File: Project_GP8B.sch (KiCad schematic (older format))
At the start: 15 parts, among them U1 74AHC05, U2 74AHC05, U3 74AHC1G04, U4 74AHC1G04, U5 74AHC05

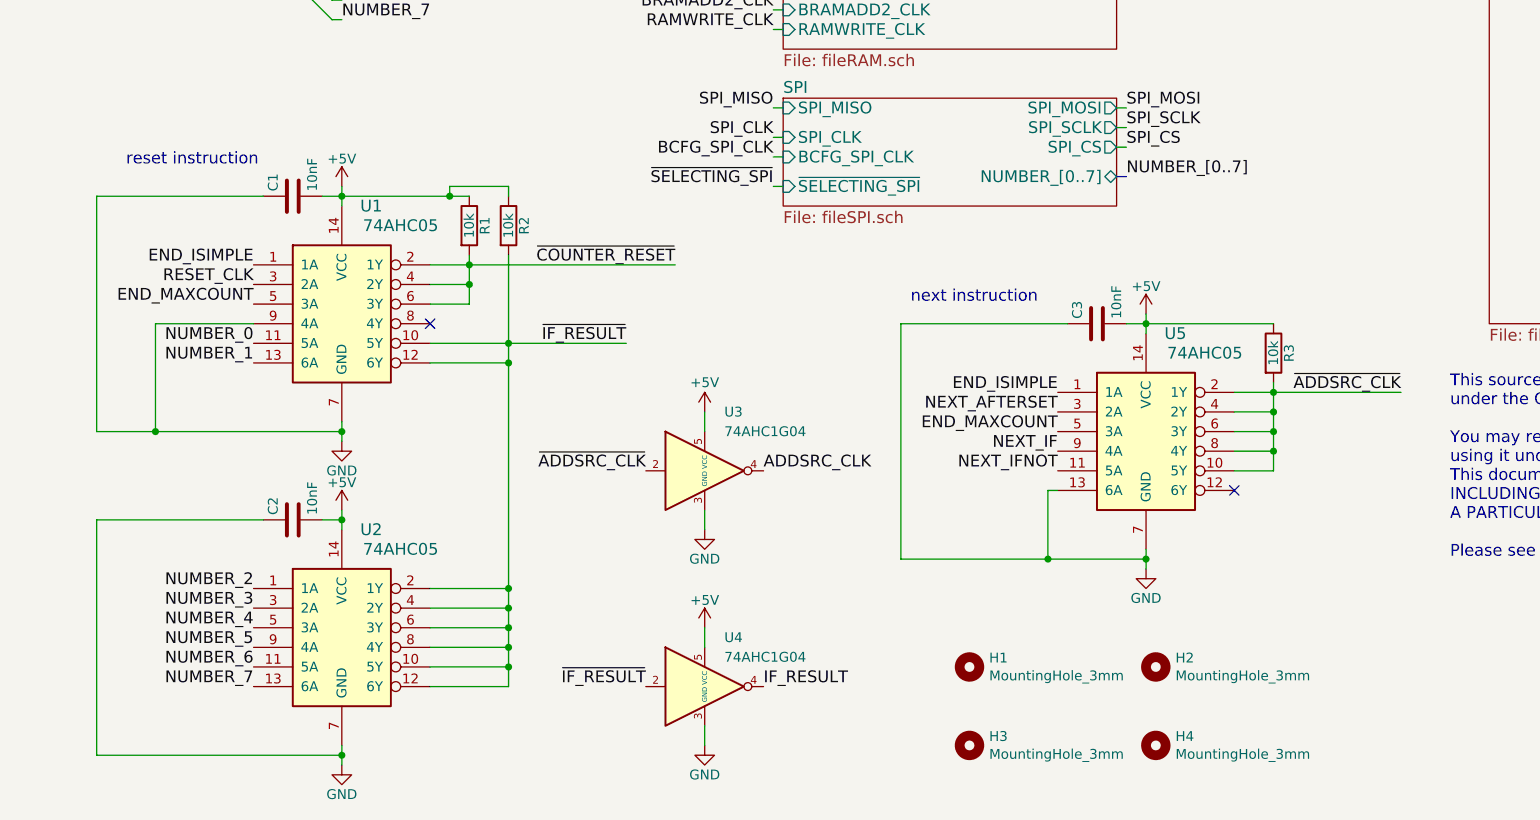
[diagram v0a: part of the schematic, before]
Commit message: Replace some gates with a 74AHC1G02 to fix the pulse problem #3
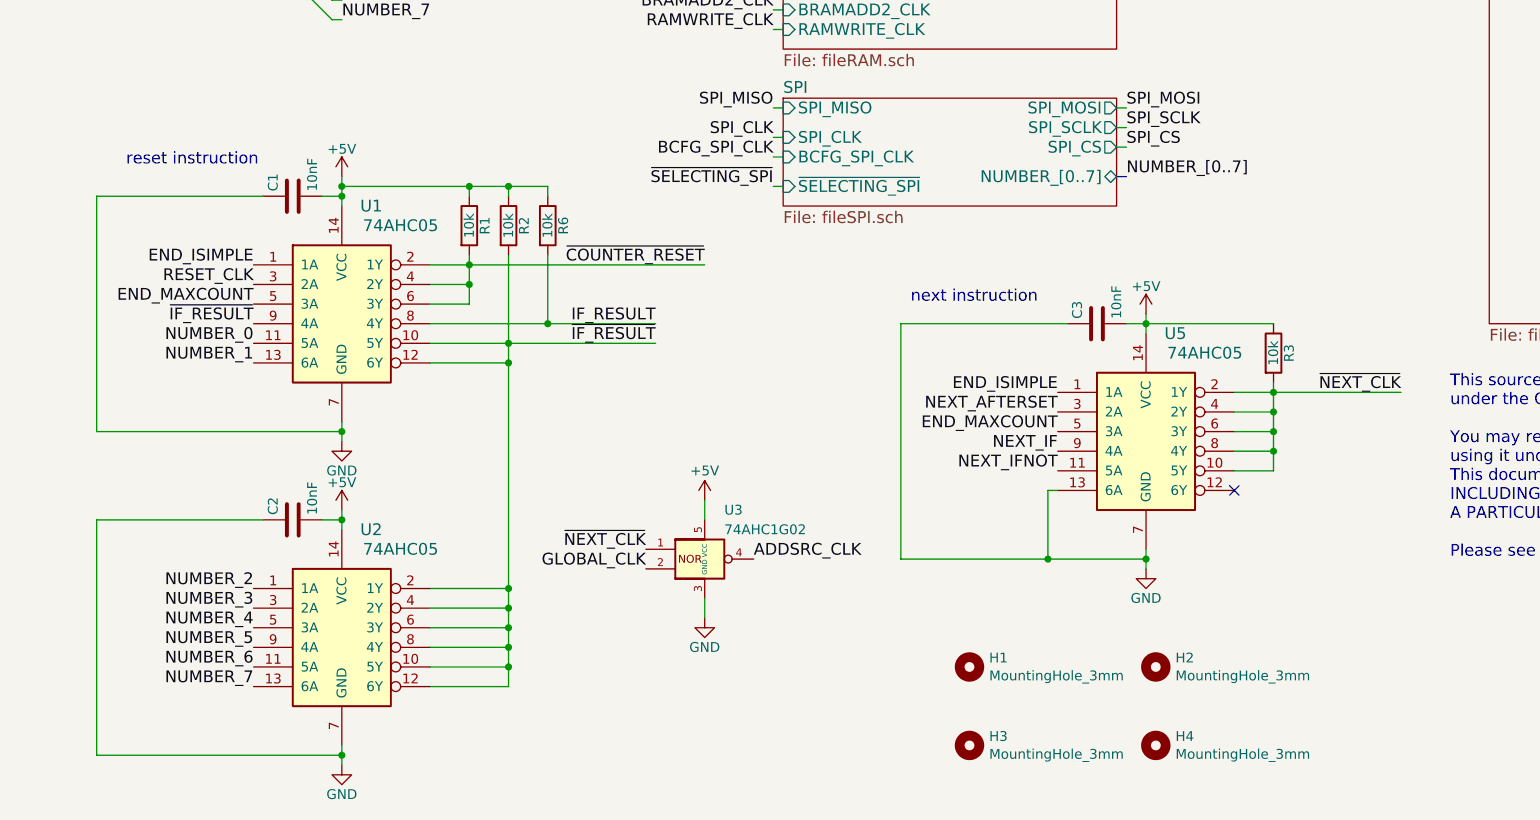
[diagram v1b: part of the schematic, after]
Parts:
- removed U3, U4: 74AHC1G04, Package_TO_SOT_SMD:SOT-23-5, symbol Custom:74AHC1G04
- added R6: 10k, Resistor_SMD:R_0805_2012Metric, symbol Device:R
- added U3: 74AHC1G02, symbol Custom:74AHC1G02
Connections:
- net +5V: now also R6.1, U3.5 (VCC)
- net ADDSRC_CLK: now also U3.4
- net GLOBAL_CLK: now also U3.2
- net GND: now also U3.3 (GND); no longer U1.9 (4A)
- net IF_RESULT: now also U1.8 (4Y), R6.2
- net ~IF_RESULT: now also U1.9 (4A)
- net ~ADDSRC_CLK renamed ~NEXT_CLK
- net ~NEXT_CLK: now also U3.1
- no-connect marks 2 -> 1
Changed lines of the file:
@@
 L power:+5V #PWR05
 U 1 1 5B109933
-P 1850 4550
-F 0 "#PWR05" H 1850 4400 50  0001 C CNN
-F 1 "+5V" H 1850 4690 50  0000 C CNN
-F 2 "" H 1850 4550 50  0001 C CNN
-F 3 "" H 1850 4550 50  0001 C CNN
-	1    1850 4550
+P 1850 4500
+F 0 "#PWR05" H 1850 4350 50  0001 C CNN
+F 1 "+5V" H 1850 4640 50  0000 C CNN
+F 2 "" H 1850 4500 50  0001 C CNN
+F 3 "" H 1850 4500 50  0001 C CNN
+	1    1850 4500
 	1    0    0    -1
 $EndComp
@@
 Text Label 1400 5050 2    60   ~ 0
 RESET_CLK
-Text Label 3550 4950 2    60   ~ 0
+Text Label 3700 4950 2    60   ~ 0
 ~COUNTER_RESET
 Text Label 1400 5350 2    60   ~ 0
@@
 	1    0    0    -1
 $EndComp
-Text Label 3300 5350 2    60   ~ 0
+Text Label 3450 5350 2    60   ~ 0
 ~IF_RESULT
 $Comp
 L power:+5V #PWR07
 U 1 1 5B155C11
-P 3700 5700
-F 0 "#PWR07" H 3700 5550 50  0001 C CNN
-F 1 "+5V" H 3700 5850 50  0000 C CNN
-F 2 "" H 3700 5700 50  0001 C CNN
-F 3 "" H 3700 5700 50  0001 C CNN
-	1    3700 5700
-	1    0    0    -1
-$EndComp
-$Comp
-L power:+5V #PWR08
-U 1 1 5B15C5EC
-P 3700 6800
-F 0 "#PWR08" H 3700 6650 50  0001 C CNN
-F 1 "+5V" H 3700 6940 50  0000 C CNN
-F 2 "" H 3700 6800 50  0001 C CNN
-F 3 "" H 3700 6800 50  0001 C CNN
-	1    3700 6800
-	1    0    0    -1
-$EndComp
-$Comp
-L power:GND #PWR09
-U 1 1 5B15D182
-P 3700 6300
-F 0 "#PWR09" H 3700 6050 50  0001 C CNN
-F 1 "GND" H 3700 6150 50  0000 C CNN
-F 2 "" H 3700 6300 50  0001 C CNN
-F 3 "" H 3700 6300 50  0001 C CNN
-	1    3700 6300
+P 3700 6150
+F 0 "#PWR07" H 3700 6000 50  0001 C CNN
+F 1 "+5V" H 3700 6300 50  0000 C CNN
+F 2 "" H 3700 6150 50  0001 C CNN
+F 3 "" H 3700 6150 50  0001 C CNN
+	1    3700 6150
 	1    0    0    -1
 $EndComp
@@
 L power:GND #PWR010
 U 1 1 5B160445
-P 3700 7400
-F 0 "#PWR010" H 3700 7150 50  0001 C CNN
-F 1 "GND" H 3700 7250 50  0000 C CNN
-F 2 "" H 3700 7400 50  0001 C CNN
-F 3 "" H 3700 7400 50  0001 C CNN
-	1    3700 7400
-	1    0    0    -1
-$EndComp
-Text Label 3400 7100 2    60   ~ 0
-~IF_RESULT
-Text Label 4000 7100 0    60   ~ 0
-IF_RESULT
+P 3700 6750
+F 0 "#PWR010" H 3700 6500 50  0001 C CNN
+F 1 "GND" H 3700 6600 50  0000 C CNN
+F 2 "" H 3700 6750 50  0001 C CNN
+F 3 "" H 3700 6750 50  0001 C CNN
+	1    3700 6750
+	1    0    0    -1
+$EndComp
 Text Label 4900 800  2    60   ~ 0
 NUMBER_[0..7]
@@
 	1850 5750 1850 5800
 Wire Wire Line
-	600  5800 900  5800
-Wire Wire Line
 	600  5800 600  4600
 Wire Wire Line
@@
 Wire Wire Line
 	2700 4600 2700 4550
-Wire Wire Line
-	2700 4550 2400 4550
-Wire Wire Line
-	2400 4550 2400 4600
-Connection ~ 2400 4600
 Wire Wire Line
 	2700 4900 2700 5350
@@
 Text Label 1350 1750 2    60   ~ 0
 ~COUNTER_RESET
-Wire Wire Line
-	1400 5250 900  5250
-Wire Wire Line
-	900  5250 900  5800
-Connection ~ 900  5800
 Text Label 10300 3300 0    60   ~ 0
 NUM_SELECT_2
@@
 Text Label 1350 2000 2    60   ~ 0
 ~SELECTING_RBEXT2
-NoConn ~ 2300 5250
 NoConn ~ 6400 6100
 Wire Bus Line
@@
 	1850 5800 1850 5850
 Wire Wire Line
-	1850 4600 2400 4600
-Wire Wire Line
 	1850 4600 1850 4650
 Wire Wire Line
 	2500 4950 2500 5050
 Wire Wire Line
-	2500 4950 3550 4950
-Wire Wire Line
 	2500 5050 2500 5150
 Wire Wire Line
-	2400 4600 2500 4600
-Wire Wire Line
 	2700 5350 2700 5450
 Wire Wire Line
-	2700 5350 3300 5350
-Wire Wire Line
 	2700 5450 2700 6600
 Wire Wire Line
@@
 Wire Wire Line
 	2700 7000 2700 7100
-Wire Wire Line
-	900  5800 1850 5800
 $Comp
 L Custom:74AHC05 U2
@@
 $EndComp
 Wire Wire Line
-	3700 5700 3700 5800
-Wire Wire Line
-	3700 6200 3700 6300
-Wire Wire Line
-	3700 6800 3700 6900
-Wire Wire Line
-	3700 7300 3700 7400
+	3700 6650 3700 6750
 Wire Wire Line
 	4050 2550 4100 2550
@@
 $EndSheet
 Text Label 7250 5600 2    60   ~ 0
-~ADDSRC_CLK
-Text Label 3400 6000 2    60   ~ 0
-~ADDSRC_CLK
-Text Label 4000 6000 0    60   ~ 0
-ADDSRC_CLK
+~NEXT_CLK
 $Sheet
 S 4100 4100 1700 550
@@
 F23 "SPI_CS" I L 1400 2350 60
 $EndSheet
-$Comp
-L Custom:74AHC1G04 U4
-U 1 1 5F3E18E2
-P 3700 7100
-F 0 "U4" H 3800 7350 50  0000 L CNN
-F 1 "74AHC1G04" H 3800 7250 50  0000 L CNN
-F 2 "Package_TO_SOT_SMD:SOT-23-5" H 3700 7100 50  0001 C CNN
-F 3 "https://assets.nexperia.com/documents/data-sheet/74AHC_AHCT1G04.pdf" H 3700 7100 50  0001 C CNN
-	1    3700 7100
-	1    0    0    -1
-$EndComp
-$Comp
-L Custom:74AHC1G04 U3
-U 1 1 5F3E1C89
-P 3700 6000
-F 0 "U3" H 3800 6300 50  0000 L CNN
-F 1 "74AHC1G04" H 3800 6200 50  0000 L CNN
-F 2 "Package_TO_SOT_SMD:SOT-23-5" H 3700 6000 50  0001 C CNN
-F 3 "https://assets.nexperia.com/documents/data-sheet/74AHC_AHCT1G04.pdf" H 3700 6000 50  0001 C CNN
-	1    3700 6000
-	1    0    0    -1
-$EndComp
+Wire Wire Line
+	600  5800 1850 5800
+Text Label 1400 5250 2    60   ~ 0
+~IF_RESULT
+Text Label 3450 5250 2    60   ~ 0
+IF_RESULT
+$Comp
+L Device:R R6
+U 1 1 604EFD65
+P 2900 4750
+F 0 "R6" V 2980 4750 50  0000 C CNN
+F 1 "10k" V 2900 4750 50  0000 C CNN
+F 2 "Resistor_SMD:R_0805_2012Metric" V 2830 4750 50  0001 C CNN
+F 3 "" H 2900 4750 50  0001 C CNN
+	1    2900 4750
+	1    0    0    -1
+$EndComp
+Wire Wire Line
+	1850 4550 2500 4550
+Wire Wire Line
+	1850 4550 1850 4500
+Connection ~ 1850 4550
+Wire Wire Line
+	2500 4600 2500 4550
+Connection ~ 2500 4550
+Wire Wire Line
+	2500 4550 2700 4550
+Wire Wire Line
+	2900 4600 2900 4550
+Wire Wire Line
+	2900 4550 2700 4550
+Connection ~ 2700 4550
+Wire Wire Line
+	2900 4900 2900 5250
+Wire Wire Line
+	2900 5250 2300 5250
+Wire Wire Line
+	2700 5350 3450 5350
+Wire Wire Line
+	3450 5250 2900 5250
+Connection ~ 2900 5250
+Wire Wire Line
+	2500 4950 3700 4950
+Text Label 3400 6500 2    60   ~ 0
+GLOBAL_CLK
+Text Label 3950 6450 0    60   ~ 0
+ADDSRC_CLK
+Text Label 3400 6400 2    60   ~ 0
+~NEXT_CLK
+$Comp
+L Custom:74AHC1G02 U3
+U 1 1 605F1C2D
+P 3700 6450
+F 0 "U3" H 3800 6700 50  0000 L CNN
+F 1 "74AHC1G02" H 3800 6600 50  0000 L CNN
+F 2 "" H 3700 6450 50  0001 C CNN
+F 3 "https://assets.nexperia.com/documents/data-sheet/74AHC_AHCT1G02.pdf" H 3700 6450 50  0001 C CNN
+	1    3700 6450
+	1    0    0    -1
+$EndComp
+Wire Wire Line
+	3700 6150 3700 6250
 Wire Bus Line
 	1700 2800 1700 3600

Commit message: Go next only if SRCVALUE, (simple instruction)
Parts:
- added R?: 10k, Resistor_SMD:R_0805_2012Metric, symbol Device:R
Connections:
- net +5V: now also R?.1
- net END_ISIMPLE: no longer U5.1 (1A)
- net GND: no longer U5.13 (6A)
- net SELECTING_SRC: now reaches U5.12 (6Y)
- net SELECTING_SRC: now also R?.2
- new net NEXT_ISIMPLE: U5.1 (1A)
- new net ~SELECTING_SRC: U5.13 (6A)
- no-connect marks 1 -> 0
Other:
- moved on the sheet: C3, R3, U3, U5
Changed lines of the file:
@@
 Comment4 ""
 $EndDescr
-Text Notes 4750 5150 0    60   ~ 0
+Text Notes 4550 5000 0    60   ~ 0
 next instruction
 $Comp
 L power:+5V #PWR01
 U 1 1 593930EA
-P 5950 5200
-F 0 "#PWR01" H 5950 5050 50  0001 C CNN
-F 1 "+5V" H 5950 5340 50  0000 C CNN
-F 2 "" H 5950 5200 50  0001 C CNN
-F 3 "" H 5950 5200 50  0001 C CNN
-	1    5950 5200
+P 5750 5000
+F 0 "#PWR01" H 5750 4850 50  0001 C CNN
+F 1 "+5V" H 5750 5140 50  0000 C CNN
+F 2 "" H 5750 5000 50  0001 C CNN
+F 3 "" H 5750 5000 50  0001 C CNN
+	1    5750 5000
 	1    0    0    -1
 $EndComp
@@
 L power:GND #PWR02
 U 1 1 593930F0
-P 5950 6500
-F 0 "#PWR02" H 5950 6250 50  0001 C CNN
-F 1 "GND" H 5950 6350 50  0000 C CNN
-F 2 "" H 5950 6500 50  0001 C CNN
-F 3 "" H 5950 6500 50  0001 C CNN
-	1    5950 6500
+P 5750 6350
+F 0 "#PWR02" H 5750 6100 50  0001 C CNN
+F 1 "GND" H 5750 6200 50  0000 C CNN
+F 2 "" H 5750 6350 50  0001 C CNN
+F 3 "" H 5750 6350 50  0001 C CNN
+	1    5750 6350
 	1    0    0    -1
 $EndComp
@@
 L Device:C C3
 U 1 1 593930F6
-P 5700 5250
-F 0 "C3" H 5725 5350 50  0000 L CNN
-F 1 "10nF" H 5725 5150 50  0000 L CNN
-F 2 "Capacitor_SMD:C_0805_2012Metric" H 5738 5100 50  0001 C CNN
-F 3 "" H 5700 5250 50  0001 C CNN
-	1    5700 5250
+P 5500 5100
+F 0 "C3" H 5525 5200 50  0000 L CNN
+F 1 "10nF" H 5525 5000 50  0000 L CNN
+F 2 "Capacitor_SMD:C_0805_2012Metric" H 5538 4950 50  0001 C CNN
+F 3 "" H 5500 5100 50  0001 C CNN
+	1    5500 5100
 	0    -1   -1   0
 $EndComp
@@
 F12 "~SELECTING_RBEXT2" O R 10250 1000 60
 F13 "~SELECTING_SPI" O R 10250 1100 60
+F14 "~SELECTING_SRC" O R 10250 1250 60
 $EndSheet
 $Sheet
@@
 L Device:R R3
 U 1 1 5B0C581A
-P 6600 5400
-F 0 "R3" V 6680 5400 50  0000 C CNN
-F 1 "10k" V 6600 5400 50  0000 C CNN
-F 2 "Resistor_SMD:R_0805_2012Metric" V 6530 5400 50  0001 C CNN
-F 3 "" H 6600 5400 50  0001 C CNN
-	1    6600 5400
+P 6400 5250
+F 0 "R3" V 6480 5250 50  0000 C CNN
+F 1 "10k" V 6400 5250 50  0000 C CNN
+F 2 "Resistor_SMD:R_0805_2012Metric" V 6330 5250 50  0001 C CNN
+F 3 "" H 6400 5250 50  0001 C CNN
+	1    6400 5250
 	1    0    0    -1
 $EndComp
@@
 L power:+5V #PWR07
 U 1 1 5B155C11
-P 3700 6150
-F 0 "#PWR07" H 3700 6000 50  0001 C CNN
-F 1 "+5V" H 3700 6300 50  0000 C CNN
-F 2 "" H 3700 6150 50  0001 C CNN
-F 3 "" H 3700 6150 50  0001 C CNN
-	1    3700 6150
+P 3650 6200
+F 0 "#PWR07" H 3650 6050 50  0001 C CNN
+F 1 "+5V" H 3650 6350 50  0000 C CNN
+F 2 "" H 3650 6200 50  0001 C CNN
+F 3 "" H 3650 6200 50  0001 C CNN
+	1    3650 6200
 	1    0    0    -1
 $EndComp
@@
 L power:GND #PWR010
 U 1 1 5B160445
-P 3700 6750
-F 0 "#PWR010" H 3700 6500 50  0001 C CNN
-F 1 "GND" H 3700 6600 50  0000 C CNN
-F 2 "" H 3700 6750 50  0001 C CNN
-F 3 "" H 3700 6750 50  0001 C CNN
-	1    3700 6750
+P 3650 6800
+F 0 "#PWR010" H 3650 6550 50  0001 C CNN
+F 1 "GND" H 3650 6650 50  0000 C CNN
+F 2 "" H 3650 6800 50  0001 C CNN
+F 3 "" H 3650 6800 50  0001 C CNN
+	1    3650 6800
 	1    0    0    -1
 $EndComp
@@
 BREAD2_[0..7]
 Wire Wire Line
-	5950 6400 5950 6450
-Wire Wire Line
-	4700 6450 4700 5250
-Wire Wire Line
-	4700 5250 5550 5250
-Connection ~ 5950 6450
-Wire Wire Line
-	5850 5250 5950 5250
-Wire Wire Line
-	5950 5200 5950 5250
-Connection ~ 5950 5250
-Wire Wire Line
-	6600 5550 6600 5600
-Wire Wire Line
-	6400 5600 6600 5600
-Wire Wire Line
-	6600 5700 6400 5700
-Connection ~ 6600 5600
-Wire Wire Line
-	6600 5800 6400 5800
-Connection ~ 6600 5700
-Wire Wire Line
-	6600 5900 6400 5900
-Connection ~ 6600 5800
-Wire Wire Line
-	6600 6000 6400 6000
-Connection ~ 6600 5900
+	5750 6250 5750 6300
+Wire Wire Line
+	4500 6300 4500 5100
+Wire Wire Line
+	4500 5100 5350 5100
+Connection ~ 5750 6300
+Wire Wire Line
+	5650 5100 5750 5100
+Wire Wire Line
+	5750 5050 5750 5100
+Connection ~ 5750 5100
+Wire Wire Line
+	6400 5400 6400 5450
+Wire Wire Line
+	6200 5450 6400 5450
+Wire Wire Line
+	6400 5550 6200 5550
+Connection ~ 6400 5450
+Wire Wire Line
+	6400 5650 6200 5650
+Connection ~ 6400 5550
+Wire Wire Line
+	6400 5750 6200 5750
+Connection ~ 6400 5650
+Wire Wire Line
+	6400 5850 6200 5850
+Connection ~ 6400 5750
 Wire Wire Line
 	1850 7400 1850 7450
@@
 Text Label 1350 2000 2    60   ~ 0
 ~SELECTING_RBEXT2
-NoConn ~ 6400 6100
 Wire Bus Line
 	6700 950  6650 950
@@
 	10300 4900 10250 4900
 Wire Wire Line
-	5950 6450 5950 6500
-Wire Wire Line
-	5950 5250 6600 5250
-Wire Wire Line
-	5950 5250 5950 5300
-Wire Wire Line
-	6600 5600 6600 5700
-Wire Wire Line
-	6600 5700 6600 5800
-Wire Wire Line
-	6600 5800 6600 5900
-Wire Wire Line
-	6600 5900 6600 6000
+	5750 6300 5750 6350
+Wire Wire Line
+	5750 5100 5750 5150
+Wire Wire Line
+	6400 5450 6400 5550
+Wire Wire Line
+	6400 5550 6400 5650
+Wire Wire Line
+	6400 5650 6400 5750
+Wire Wire Line
+	6400 5750 6400 5850
 Wire Wire Line
 	1850 7450 1850 7500
@@
 L Custom:74AHC05 U5
 U 1 1 5C936C17
-P 5950 5800
-F 0 "U5" H 6100 6300 60  0000 C CNN
-F 1 "74AHC05" H 6250 6200 60  0000 C CNN
-F 2 "Package_SO:SOIC-14_3.9x8.7mm_P1.27mm" H 5750 6100 60  0001 C CNN
-F 3 "" H 5750 6100 60  0001 C CNN
-	1    5950 5800
-	1    0    0    -1
-$EndComp
-Wire Wire Line
-	3700 6650 3700 6750
+P 5750 5650
+F 0 "U5" H 5900 6150 60  0000 C CNN
+F 1 "74AHC05" H 6050 6050 60  0000 C CNN
+F 2 "Package_SO:SOIC-14_3.9x8.7mm_P1.27mm" H 5550 5950 60  0001 C CNN
+F 3 "" H 5550 5950 60  0001 C CNN
+	1    5750 5650
+	1    0    0    -1
+$EndComp
+Wire Wire Line
+	3650 6700 3650 6800
 Wire Wire Line
 	4050 2550 4100 2550
@@
 Wire Wire Line
 	7700 2350 7650 2350
-Wire Wire Line
-	6600 5600 7250 5600
 Text Label 4050 2300 2    60   ~ 0
 NUMBER_[0..7]
@@
 F33 "OPCHOOSE_CLK" O R 10250 2500 60
 F34 "BCFG_SPI_CLK" O R 10250 5150 60
+F35 "NEXT_ISIMPLE" O R 10250 3750 60
+F36 "SELECTING_SRC" I L 7700 2800 60
 $EndSheet
-Text Label 7250 5600 2    60   ~ 0
+Text Label 7300 5450 2    60   ~ 0
 ~NEXT_CLK
 $Sheet
@@
 Text Label 4050 3650 2    60   ~ 0
 BRAMADD2_CLK
-Text Label 5500 5600 2    60   ~ 0
-END_ISIMPLE
-Text Label 5500 5700 2    60   ~ 0
+Text Label 5300 5550 2    60   ~ 0
 NEXT_AFTERSET
-Text Label 5500 5800 2    60   ~ 0
+Text Label 5300 5650 2    60   ~ 0
 END_MAXCOUNT
-Text Label 5500 5900 2    60   ~ 0
+Text Label 5300 5750 2    60   ~ 0
 NEXT_IF
-Text Label 5500 6000 2    60   ~ 0
+Text Label 5300 5850 2    60   ~ 0
 NEXT_IFNOT
 Text Label 1400 4950 2    60   ~ 0
@@
 Text Label 1400 5150 2    60   ~ 0
 END_MAXCOUNT
-Wire Wire Line
-	4700 6450 5450 6450
-Wire Wire Line
-	5500 6100 5450 6100
-Wire Wire Line
-	5450 6100 5450 6450
-Connection ~ 5450 6450
-Wire Wire Line
-	5450 6450 5950 6450
 Text Label 10300 5150 0    60   ~ 0
 BCFG_SPI_CLK
@@
 Wire Wire Line
 	2500 4950 3700 4950
-Text Label 3400 6500 2    60   ~ 0
+Text Label 3350 6550 2    60   ~ 0
 GLOBAL_CLK
-Text Label 3950 6450 0    60   ~ 0
+Text Label 3900 6500 0    60   ~ 0
 ADDSRC_CLK
-Text Label 3400 6400 2    60   ~ 0
+Text Label 3350 6450 2    60   ~ 0
 ~NEXT_CLK
 $Comp
 L Custom:74AHC1G02 U3
 U 1 1 605F1C2D
-P 3700 6450
-F 0 "U3" H 3800 6700 50  0000 L CNN
-F 1 "74AHC1G02" H 3800 6600 50  0000 L CNN
-F 2 "" H 3700 6450 50  0001 C CNN
-F 3 "https://assets.nexperia.com/documents/data-sheet/74AHC_AHCT1G02.pdf" H 3700 6450 50  0001 C CNN
-	1    3700 6450
-	1    0    0    -1
-$EndComp
-Wire Wire Line
-	3700 6150 3700 6250
+P 3650 6500
+F 0 "U3" H 3750 6750 50  0000 L CNN
+F 1 "74AHC1G02" H 3750 6650 50  0000 L CNN
+F 2 "" H 3650 6500 50  0001 C CNN
+F 3 "https://assets.nexperia.com/documents/data-sheet/74AHC_AHCT1G02.pdf" H 3650 6500 50  0001 C CNN
+	1    3650 6500
+	1    0    0    -1
+$EndComp
+Wire Wire Line
+	3650 6200 3650 6300
+Text Label 10300 1250 0    60   ~ 0
+~SELECTING_SRC
+Wire Wire Line
+	10300 1250 10250 1250
+Text Label 10300 3750 0    60   ~ 0
+NEXT_ISIMPLE
+Wire Wire Line
+	10300 3750 10250 3750
+Wire Wire Line
+	7650 2800 7700 2800
+Text Label 5300 5450 2    60   ~ 0
+NEXT_ISIMPLE
+Text Label 5300 5950 2    60   ~ 0
+~SELECTING_SRC
+Wire Wire Line
+	4500 6300 5750 6300
+Text Label 7300 5950 2    60   ~ 0
+SELECTING_SRC
+$Comp
+L Device:R R?
+U 1 1 60507EBE
+P 6600 5250
+F 0 "R?" V 6680 5250 50  0000 C CNN
+F 1 "10k" V 6600 5250 50  0000 C CNN
+F 2 "Resistor_SMD:R_0805_2012Metric" V 6530 5250 50  0001 C CNN
+F 3 "" H 6600 5250 50  0001 C CNN
+	1    6600 5250
+	1    0    0    -1
+$EndComp
+Wire Wire Line
+	6600 5400 6600 5950
+Wire Wire Line
+	6600 5950 6200 5950
+Wire Wire Line
+	6600 5100 6600 5050
+Wire Wire Line
+	6600 5050 6400 5050
+Wire Wire Line
+	5750 5000 5750 5050
+Connection ~ 5750 5050
+Wire Wire Line
+	6400 5100 6400 5050
+Connection ~ 6400 5050
+Wire Wire Line
+	6400 5050 5750 5050
+Wire Wire Line
+	6400 5450 7300 5450
+Wire Wire Line
+	6600 5950 7300 5950
+Connection ~ 6600 5950
+Text Label 7650 2800 2    60   ~ 0
+SELECTING_SRC
 Wire Bus Line
 	1700 2800 1700 3600
